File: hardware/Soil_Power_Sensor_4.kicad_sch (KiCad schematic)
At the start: 15 parts, among them J3 UART, J5 Micro_SD_Card, SW1 BOOT, SW2 EN, U8 ESP32-C3-WROOM-02-N4

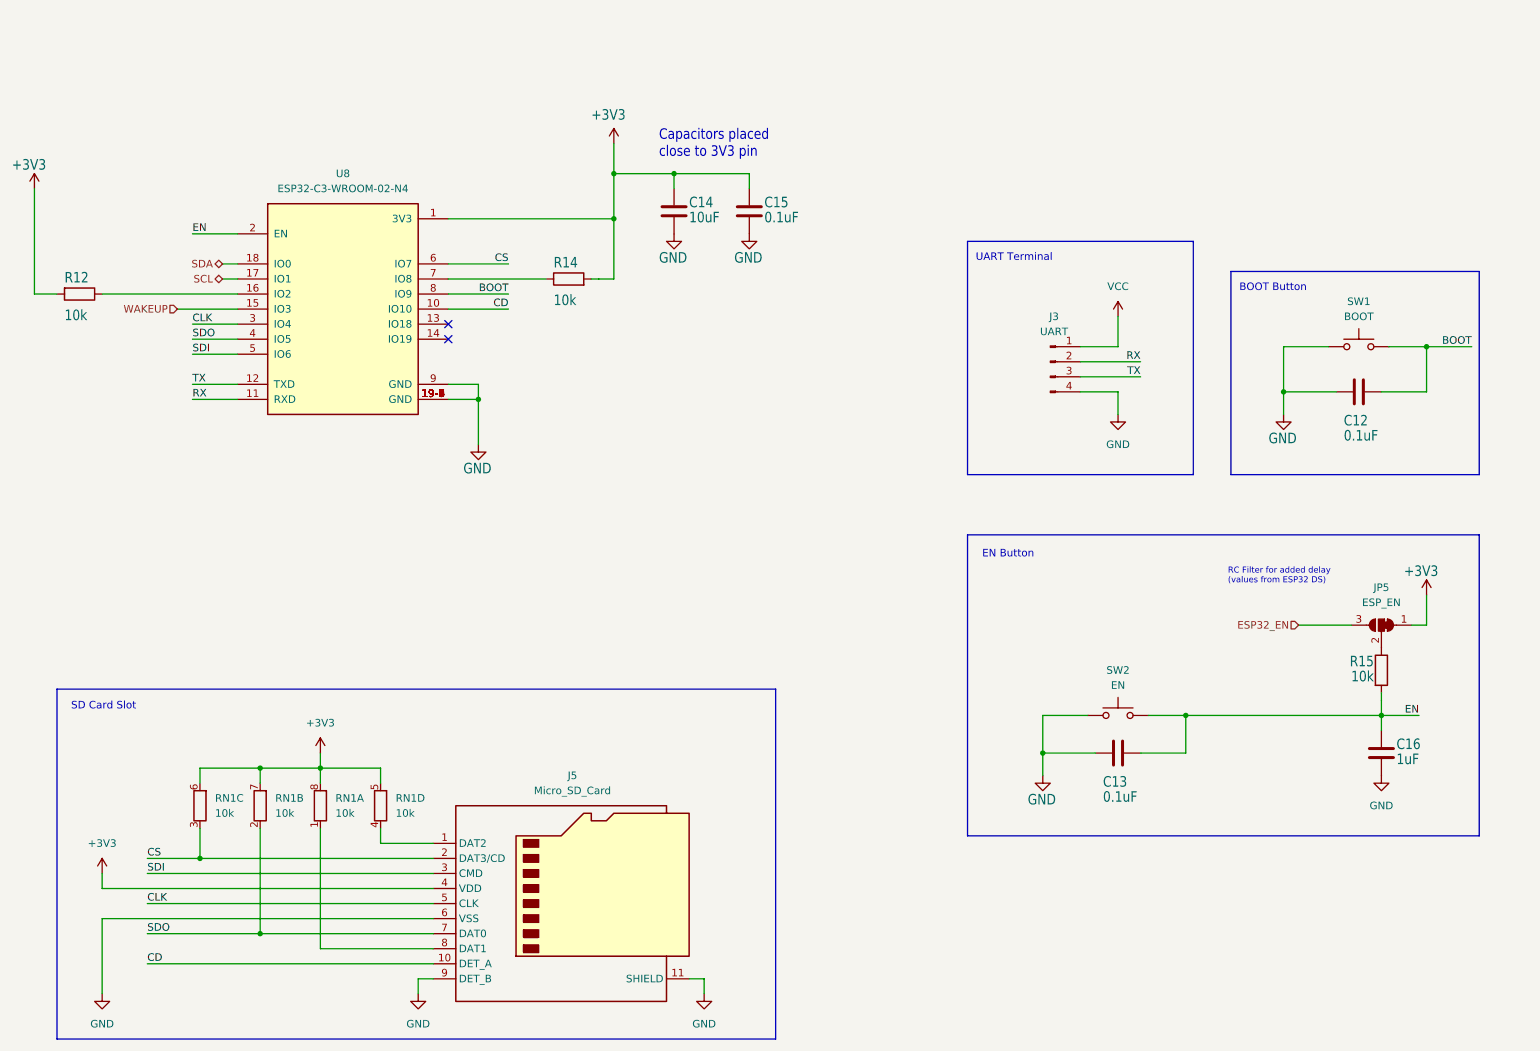
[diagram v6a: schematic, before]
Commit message: Updated debug header
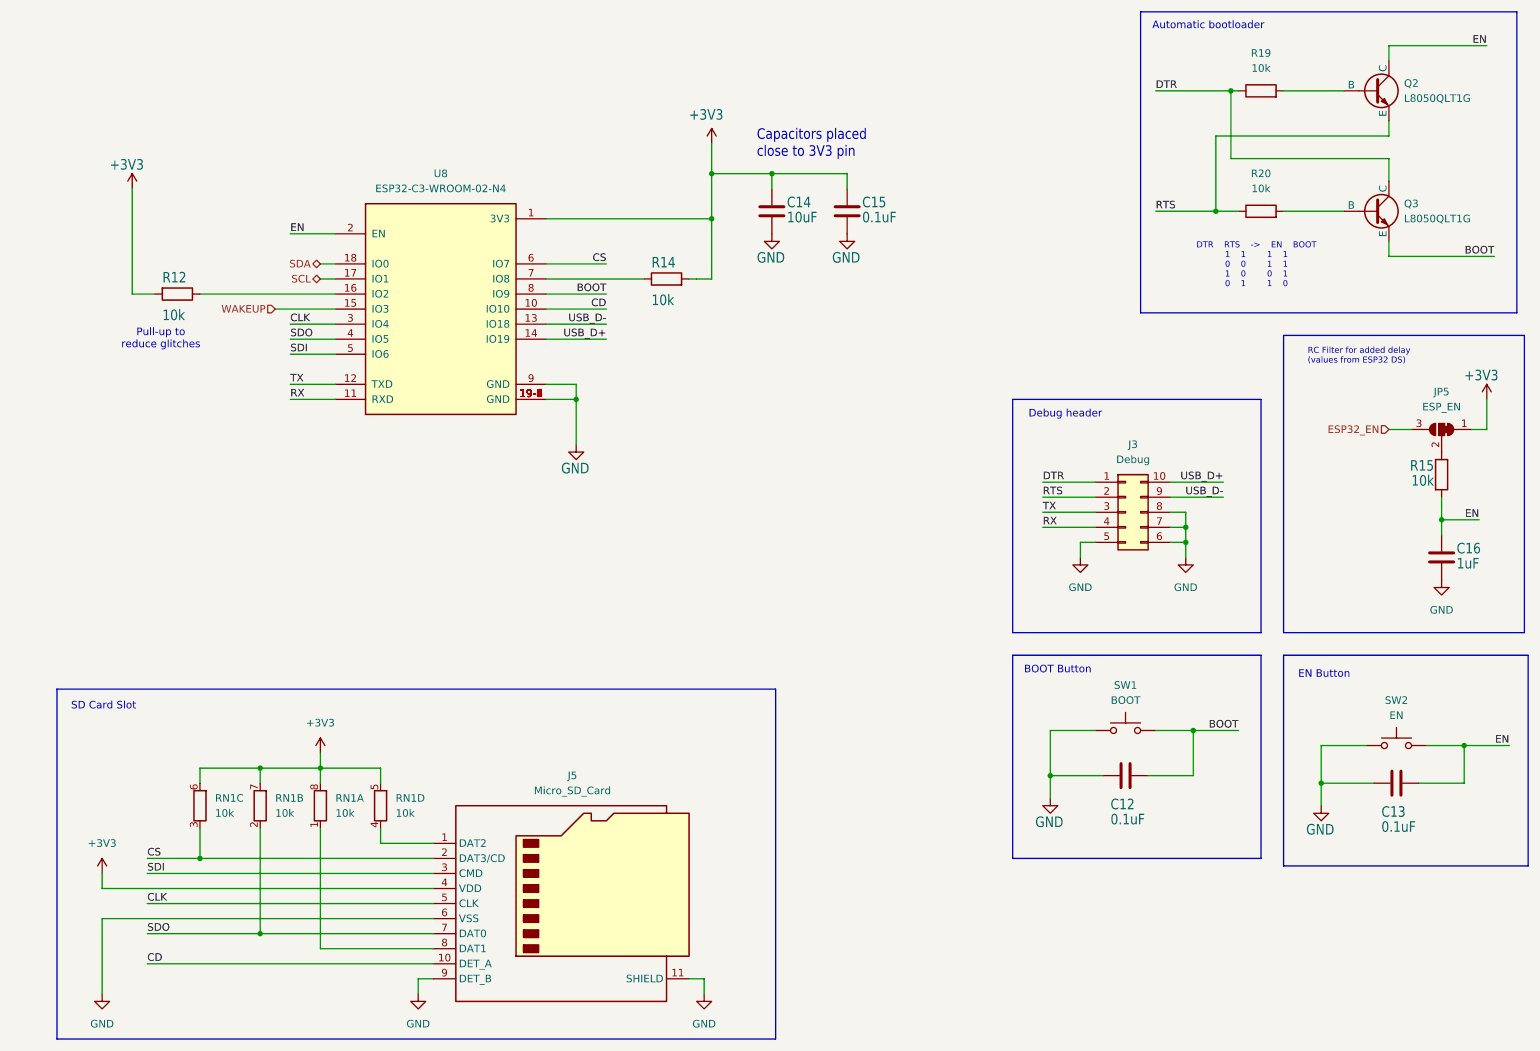
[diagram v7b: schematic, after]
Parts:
- removed J3: UART, Connector_PinHeader_2.54mm:PinHeader_1x04_P2.54mm_Vertical, symbol Connector:Conn_01x04_Pin
- added J3: Debug, symbol Connector_Generic:Conn_02x05_Counter_Clockwise
- added Q2, Q3: L8050QLT1G, Package_TO_SOT_SMD:SOT-23, symbol Simulation_SPICE:NPN
- added R19, R20: 10k, Resistor_SMD:R_0603_1608Metric, symbol Device:R
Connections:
- net BOOT: now also Q3.3 (E)
- net EN: now also Q2.1 (C)
- net GND: now also J3.5 (Pin_5), J3.6 (Pin_6), J3.7 (Pin_7), J3.8 (Pin_8)
- net RX: now also J3.4 (Pin_4)
- net TX: now also J3.3 (Pin_3)
- net USB_D-: now reaches U8.13 (IO18)
- net USB_D-: now also J3.9 (Pin_9)
- net USB_D+: now reaches U8.14 (IO19)
- net USB_D+: now also J3.10 (Pin_10)
- new net: Q2.2 (B), R19.2
- new net: Q3.2 (B), R20.2
- new net DTR: J3.1 (Pin_1), Q3.1 (C), R19.1
- new net RTS: J3.2 (Pin_2), Q2.3 (E), R20.1
- no-connect marks 2 -> 0
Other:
- note added: "Automatic bootloader"
- note added: "DTR RTS -> EN BOOT 1 1 1 1 0 0 1 1 1 0 0 1 0 1 1 0"
- note added: "Debug header"
- note added: "Pull-up to reduce glitches"
- note removed: "UART Terminal"
- moved on the sheet: C12, C13, C14, C15, C16, JP5, R12, R14, R15, SW1, SW2, U8

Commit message: Routed PCB
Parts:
- J3: footprint (none) -> Connector_PinHeader_2.54mm:PinHeader_2x05_P2.54mm_Vertical; symbol Connector_Generic:Conn_02x05_Counter_Clockwise -> Connector_Generic:Conn_02x05_Odd_Even
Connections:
- net BOOT: now also Q3.1 (C); no longer Q3.3 (E)
- net DTR: now also Q3.3 (E); no longer Q3.1 (C)
- net GND: now also J3.10 (Pin_10), J3.9 (Pin_9); no longer J3.5 (Pin_5), J3.7 (Pin_7)
- net RTS: now also J3.3 (Pin_3); no longer J3.2 (Pin_2)
- net RX: now also J3.7 (Pin_7); no longer J3.4 (Pin_4)
- net TX: now also J3.5 (Pin_5); no longer J3.3 (Pin_3)
- net USB_D+: now also J3.2 (Pin_2); no longer J3.10 (Pin_10)
- net USB_D-: now also J3.4 (Pin_4); no longer J3.9 (Pin_9)
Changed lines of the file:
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@@
 	)
 	(symbol
-		(lib_id "Connector_Generic:Conn_02x05_Counter_Clockwise")
+		(lib_id "Connector_Generic:Conn_02x05_Odd_Even")
 		(at 210.82 101.6 0)
 		(unit 1)
@@
 			)
 		)
-		(property "Footprint" ""
+		(property "Footprint" "Connector_PinHeader_2.54mm:PinHeader_2x05_P2.54mm_Vertical"
 			(at 210.82 101.6 0)
 			(effects
@@
 			)
 		)
-		(property "Description" "Generic connector, double row, 02x05, counter clockwise pin numbering scheme (similar to DIP package numbering), script generated (kicad-library-utils/schlib/autogen/connector/)"
+		(property "Description" "Generic connector, double row, 02x05, odd/even pin numbering scheme (row 1 odd numbers, row 2 even numbers), script generated (kicad-library-utils/schlib/autogen/connector/)"
 			(at 210.82 101.6 0)
 			(effects
@@
 		(lib_id "Simulation_SPICE:NPN")
 		(at 252.73 50.8 0)
-		(unit 1)
-		(exclude_from_sim no)
-		(in_bom yes)
-		(on_board yes)
-		(dnp no)
-		(fields_autoplaced yes)
+		(mirror x)
+		(unit 1)
+		(exclude_from_sim no)
+		(in_bom yes)
+		(on_board yes)
+		(dnp no)
 		(property "Reference" "Q3"
-			(at 257.81 49.5299 0)
+			(at 257.81 52.0701 0)
 			(effects
 				(font
@@
 		)
 		(property "Value" "L8050QLT1G"
-			(at 257.81 52.0699 0)
-			(effects
-				(font
+			(at 257.81 49.5301 0)
+			(effects
+				(font
